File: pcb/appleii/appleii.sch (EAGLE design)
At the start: 21 parts, among them J1 ATX24RH

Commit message: updated IIGS design
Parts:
- added U$14, U$15, U$16, U$17, U$18, U$19, U$20: EDGEPAD, atx4vc:EDGEPAD
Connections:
- net GND: now also U$14.P$1, U$15.P$1, U$16.P$1, U$17.P$1, U$18.P$1, U$19.P$1, U$20.P$1
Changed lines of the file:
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@@
 <part name="U$13" library="atx4vc" deviceset="EDGEPAD" device=""/>
 <part name="GND15" library="supply1" library_urn="urn:adsk.eagle:library:371" deviceset="GND" device=""/>
+<part name="U$14" library="atx4vc" deviceset="EDGEPAD" device=""/>
+<part name="GND16" library="supply1" library_urn="urn:adsk.eagle:library:371" deviceset="GND" device=""/>
+<part name="U$15" library="atx4vc" deviceset="EDGEPAD" device=""/>
+<part name="GND17" library="supply1" library_urn="urn:adsk.eagle:library:371" deviceset="GND" device=""/>
+<part name="U$16" library="atx4vc" deviceset="EDGEPAD" device=""/>
+<part name="GND18" library="supply1" library_urn="urn:adsk.eagle:library:371" deviceset="GND" device=""/>
+<part name="U$17" library="atx4vc" deviceset="EDGEPAD" device=""/>
+<part name="GND19" library="supply1" library_urn="urn:adsk.eagle:library:371" deviceset="GND" device=""/>
+<part name="U$18" library="atx4vc" deviceset="EDGEPAD" device=""/>
+<part name="GND20" library="supply1" library_urn="urn:adsk.eagle:library:371" deviceset="GND" device=""/>
+<part name="U$19" library="atx4vc" deviceset="EDGEPAD" device=""/>
+<part name="GND21" library="supply1" library_urn="urn:adsk.eagle:library:371" deviceset="GND" device=""/>
+<part name="U$20" library="atx4vc" deviceset="EDGEPAD" device=""/>
+<part name="GND22" library="supply1" library_urn="urn:adsk.eagle:library:371" deviceset="GND" device=""/>
 </parts>
 <sheets>
@@
 <instance part="GND15" gate="1" x="73.66" y="25.4" smashed="yes">
 <attribute name="VALUE" x="71.12" y="22.86" size="1.778" layer="96"/>
+</instance>
+<instance part="U$14" gate="G$1" x="175.26" y="53.34" smashed="yes"/>
+<instance part="GND16" gate="1" x="165.1" y="50.8" smashed="yes">
+<attribute name="VALUE" x="162.56" y="48.26" size="1.778" layer="96"/>
+</instance>
+<instance part="U$15" gate="G$1" x="175.26" y="40.64" smashed="yes"/>
+<instance part="GND17" gate="1" x="165.1" y="38.1" smashed="yes">
+<attribute name="VALUE" x="162.56" y="35.56" size="1.778" layer="96"/>
+</instance>
+<instance part="U$16" gate="G$1" x="175.26" y="27.94" smashed="yes"/>
+<instance part="GND18" gate="1" x="165.1" y="25.4" smashed="yes">
+<attribute name="VALUE" x="162.56" y="22.86" size="1.778" layer="96"/>
+</instance>
+<instance part="U$17" gate="G$1" x="175.26" y="15.24" smashed="yes"/>
+<instance part="GND19" gate="1" x="165.1" y="12.7" smashed="yes">
+<attribute name="VALUE" x="162.56" y="10.16" size="1.778" layer="96"/>
+</instance>
+<instance part="U$18" gate="G$1" x="261.62" y="35.56" smashed="yes"/>
+<instance part="GND20" gate="1" x="251.46" y="33.02" smashed="yes">
+<attribute name="VALUE" x="248.92" y="30.48" size="1.778" layer="96"/>
+</instance>
+<instance part="U$19" gate="G$1" x="261.62" y="22.86" smashed="yes"/>
+<instance part="GND21" gate="1" x="251.46" y="20.32" smashed="yes">
+<attribute name="VALUE" x="248.92" y="17.78" size="1.778" layer="96"/>
+</instance>
+<instance part="U$20" gate="G$1" x="261.62" y="10.16" smashed="yes"/>
+<instance part="GND22" gate="1" x="251.46" y="7.62" smashed="yes">
+<attribute name="VALUE" x="248.92" y="5.08" size="1.778" layer="96"/>
 </instance>
 </instances>
@@
 <wire x1="73.66" y1="27.94" x2="78.74" y2="27.94" width="0.1524" layer="91"/>
 </segment>
+<segment>
+<pinref part="GND16" gate="1" pin="GND"/>
+<pinref part="U$14" gate="G$1" pin="P$1"/>
+<wire x1="165.1" y1="53.34" x2="170.18" y2="53.34" width="0.1524" layer="91"/>
+</segment>
+<segment>
+<pinref part="GND17" gate="1" pin="GND"/>
+<pinref part="U$15" gate="G$1" pin="P$1"/>
+<wire x1="165.1" y1="40.64" x2="170.18" y2="40.64" width="0.1524" layer="91"/>
+</segment>
+<segment>
+<pinref part="GND18" gate="1" pin="GND"/>
+<pinref part="U$16" gate="G$1" pin="P$1"/>
+<wire x1="165.1" y1="27.94" x2="170.18" y2="27.94" width="0.1524" layer="91"/>
+</segment>
+<segment>
+<pinref part="GND19" gate="1" pin="GND"/>
+<pinref part="U$17" gate="G$1" pin="P$1"/>
+<wire x1="165.1" y1="15.24" x2="170.18" y2="15.24" width="0.1524" layer="91"/>
+</segment>
+<segment>
+<pinref part="GND20" gate="1" pin="GND"/>
+<pinref part="U$18" gate="G$1" pin="P$1"/>
+<wire x1="251.46" y1="35.56" x2="256.54" y2="35.56" width="0.1524" layer="91"/>
+</segment>
+<segment>
+<pinref part="GND21" gate="1" pin="GND"/>
+<pinref part="U$19" gate="G$1" pin="P$1"/>
+<wire x1="251.46" y1="22.86" x2="256.54" y2="22.86" width="0.1524" layer="91"/>
+</segment>
+<segment>
+<pinref part="GND22" gate="1" pin="GND"/>
+<pinref part="U$20" gate="G$1" pin="P$1"/>
+<wire x1="251.46" y1="10.16" x2="256.54" y2="10.16" width="0.1524" layer="91"/>
+</segment>
 </net>

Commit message: added more caps
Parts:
- removed C1: (no value), capacitor-wima:C5/2.5
- removed JP1: (no value), pinhead:PINHD-1X2
- added C5, C7, C8, C9: (no value), capacitor-wima:C5/2.5
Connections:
- net +12V: now also C9.1
- net +5V: now also C7.1, C8.1
- net GND: now also C5.2, C7.2, C8.2, C9.2; no longer C1.2, JP1.2
- net N$5: no longer JP1.1
- net N$6: no longer C1.1
- net N$8: now also C5.1
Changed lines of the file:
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@@
 <?xml version="1.0" encoding="utf-8"?>
 <!DOCTYPE eagle SYSTEM "eagle.dtd">
-<eagle version="9.6.1">
+<eagle version="9.6.2">
 <drawing>
 <settings>
@@
 <part name="U$1" library="atx_power_control" deviceset="CAR_FUSE_HOLDER" device="3IN1"/>
 <part name="U$2" library="atx_power_control" deviceset="CAR_FUSE_HOLDER" device="3IN1"/>
-<part name="JP1" library="pinhead" library_urn="urn:adsk.eagle:library:325" deviceset="PINHD-1X2" device="" package3d_urn="urn:adsk.eagle:package:22435/2"/>
 <part name="P+3" library="supply1" library_urn="urn:adsk.eagle:library:371" deviceset="+5V" device=""/>
 <part name="GND3" library="supply1" library_urn="urn:adsk.eagle:library:371" deviceset="GND" device=""/>
@@
 <part name="P-5" library="supply1" library_urn="urn:adsk.eagle:library:371" deviceset="-5V" device=""/>
 <part name="C2" library="capacitor-wima" library_urn="urn:adsk.eagle:library:116" deviceset="C" device="5/2.5" package3d_urn="urn:adsk.eagle:package:5426/1"/>
-<part name="C1" library="capacitor-wima" library_urn="urn:adsk.eagle:library:116" deviceset="C" device="5/2.5" package3d_urn="urn:adsk.eagle:package:5426/1"/>
-<part name="GND9" library="supply1" library_urn="urn:adsk.eagle:library:371" deviceset="GND" device=""/>
 <part name="GND10" library="supply1" library_urn="urn:adsk.eagle:library:371" deviceset="GND" device=""/>
 <part name="C3" library="capacitor-wima" library_urn="urn:adsk.eagle:library:116" deviceset="C" device="5/2.5" package3d_urn="urn:adsk.eagle:package:5426/1"/>
@@
 <part name="U$20" library="atx4vc" deviceset="EDGEPAD" device=""/>
 <part name="GND22" library="supply1" library_urn="urn:adsk.eagle:library:371" deviceset="GND" device=""/>
+<part name="C5" library="capacitor-wima" library_urn="urn:adsk.eagle:library:116" deviceset="C" device="5/2.5" package3d_urn="urn:adsk.eagle:package:5426/1"/>
+<part name="GND23" library="supply1" library_urn="urn:adsk.eagle:library:371" deviceset="GND" device=""/>
+<part name="C7" library="capacitor-wima" library_urn="urn:adsk.eagle:library:116" deviceset="C" device="5/2.5" package3d_urn="urn:adsk.eagle:package:5426/1"/>
+<part name="C8" library="capacitor-wima" library_urn="urn:adsk.eagle:library:116" deviceset="C" device="5/2.5" package3d_urn="urn:adsk.eagle:package:5426/1"/>
+<part name="GND24" library="supply1" library_urn="urn:adsk.eagle:library:371" deviceset="GND" device=""/>
+<part name="C9" library="capacitor-wima" library_urn="urn:adsk.eagle:library:116" deviceset="C" device="5/2.5" package3d_urn="urn:adsk.eagle:package:5426/1"/>
+<part name="GND25" library="supply1" library_urn="urn:adsk.eagle:library:371" deviceset="GND" device=""/>
 </parts>
 <sheets>
@@
 <instance part="U$1" gate="G$1" x="38.1" y="187.96" smashed="yes"/>
 <instance part="U$2" gate="G$1" x="154.94" y="175.26" smashed="yes"/>
-<instance part="JP1" gate="G$1" x="180.34" y="160.02" smashed="yes">
-<attribute name="NAME" x="173.99" y="165.735" size="1.778" layer="95"/>
-<attribute name="VALUE" x="173.99" y="154.94" size="1.778" layer="96"/>
-</instance>
 <instance part="P+3" gate="1" x="12.7" y="193.04" smashed="yes">
 <attribute name="VALUE" x="10.16" y="187.96" size="1.778" layer="96" rot="R90"/>
@@
 <attribute name="VALUE" x="133.604" y="168.021" size="1.778" layer="96"/>
 </instance>
-<instance part="C1" gate="G$1" x="58.42" y="185.42" smashed="yes">
-<attribute name="NAME" x="59.944" y="185.801" size="1.778" layer="95"/>
-<attribute name="VALUE" x="59.944" y="180.721" size="1.778" layer="96"/>
-</instance>
-<instance part="GND9" gate="1" x="58.42" y="177.8" smashed="yes">
-<attribute name="VALUE" x="55.88" y="175.26" size="1.778" layer="96"/>
-</instance>
 <instance part="GND10" gate="1" x="132.08" y="165.1" smashed="yes">
 <attribute name="VALUE" x="129.54" y="162.56" size="1.778" layer="96"/>
@@
 <instance part="GND22" gate="1" x="251.46" y="7.62" smashed="yes">
 <attribute name="VALUE" x="248.92" y="5.08" size="1.778" layer="96"/>
+</instance>
+<instance part="C5" gate="G$1" x="127" y="172.72" smashed="yes">
+<attribute name="NAME" x="128.524" y="173.101" size="1.778" layer="95"/>
+<attribute name="VALUE" x="128.524" y="168.021" size="1.778" layer="96"/>
+</instance>
+<instance part="GND23" gate="1" x="127" y="165.1" smashed="yes">
+<attribute name="VALUE" x="124.46" y="162.56" size="1.778" layer="96"/>
+</instance>
+<instance part="C7" gate="G$1" x="20.32" y="177.8" smashed="yes">
+<attribute name="NAME" x="21.844" y="178.181" size="1.778" layer="95"/>
+<attribute name="VALUE" x="21.844" y="173.101" size="1.778" layer="96"/>
+</instance>
+<instance part="C8" gate="G$1" x="12.7" y="177.8" smashed="yes">
+<attribute name="NAME" x="14.224" y="178.181" size="1.778" layer="95"/>
+<attribute name="VALUE" x="14.224" y="173.101" size="1.778" layer="96"/>
+</instance>
+<instance part="GND24" gate="1" x="12.7" y="167.64" smashed="yes">
+<attribute name="VALUE" x="10.16" y="165.1" size="1.778" layer="96"/>
+</instance>
+<instance part="C9" gate="G$1" x="193.04" y="172.72" smashed="yes">
+<attribute name="NAME" x="194.564" y="173.101" size="1.778" layer="95"/>
+<attribute name="VALUE" x="194.564" y="168.021" size="1.778" layer="96"/>
+</instance>
+<instance part="GND25" gate="1" x="193.04" y="165.1" smashed="yes">
+<attribute name="VALUE" x="190.5" y="162.56" size="1.778" layer="96"/>
 </instance>
 </instances>
@@
 <segment>
 <pinref part="GND3" gate="1" pin="GND"/>
-<pinref part="JP1" gate="G$1" pin="2"/>
-<wire x1="149.86" y1="160.02" x2="177.8" y2="160.02" width="0.1524" layer="91"/>
-<wire x1="177.8" y1="160.02" x2="215.9" y2="160.02" width="0.1524" layer="91"/>
+<wire x1="149.86" y1="160.02" x2="215.9" y2="160.02" width="0.1524" layer="91"/>
 <wire x1="215.9" y1="160.02" x2="215.9" y2="149.86" width="0.1524" layer="91"/>
-<junction x="177.8" y="160.02"/>
 <pinref part="U$3" gate="G$1" pin="P$3"/>
 <pinref part="U$3" gate="G$1" pin="P$1"/>
@@
 </segment>
 <segment>
-<pinref part="C1" gate="G$1" pin="2"/>
-<pinref part="GND9" gate="1" pin="GND"/>
-</segment>
-<segment>
 <pinref part="C2" gate="G$1" pin="2"/>
 <pinref part="GND10" gate="1" pin="GND"/>
@@
 <pinref part="U$20" gate="G$1" pin="P$1"/>
 <wire x1="251.46" y1="10.16" x2="256.54" y2="10.16" width="0.1524" layer="91"/>
+</segment>
+<segment>
+<pinref part="C5" gate="G$1" pin="2"/>
+<pinref part="GND23" gate="1" pin="GND"/>
+</segment>
+<segment>
+<pinref part="C8" gate="G$1" pin="2"/>
+<pinref part="GND24" gate="1" pin="GND"/>
+<wire x1="12.7" y1="172.72" x2="12.7" y2="170.18" width="0.1524" layer="91"/>
+<pinref part="C7" gate="G$1" pin="2"/>
+<wire x1="12.7" y1="172.72" x2="20.32" y2="172.72" width="0.1524" layer="91"/>
+<junction x="12.7" y="172.72"/>
+</segment>
+<segment>
+<pinref part="C9" gate="G$1" pin="2"/>
+<pinref part="GND25" gate="1" pin="GND"/>
 </segment>
 </net>
@@
 <pinref part="J1" gate="G$1" pin="5V@3"/>
 <pinref part="J1" gate="G$1" pin="5V@4"/>
-<pinref part="C1" gate="G$1" pin="1"/>
-<wire x1="53.594" y1="189.23" x2="58.42" y2="189.23" width="0.1524" layer="91"/>
-<wire x1="58.42" y1="189.23" x2="58.42" y2="187.96" width="0.1524" layer="91"/>
 </segment>
 </net>
@@
 <wire x1="12.7" y1="189.23" x2="12.7" y2="190.5" width="0.1524" layer="91"/>
 <junction x="23.114" y="189.23"/>
+<pinref part="C8" gate="G$1" pin="1"/>
+<wire x1="12.7" y1="180.34" x2="12.7" y2="190.5" width="0.1524" layer="91"/>
+<junction x="12.7" y="190.5"/>
+<pinref part="C7" gate="G$1" pin="1"/>
+<wire x1="20.32" y1="180.34" x2="12.7" y2="180.34" width="0.1524" layer="91"/>
+<junction x="12.7" y="180.34"/>
 </segment>
 <segment>
@@
 <pinref part="J1" gate="G$1" pin="12V@1"/>
 <pinref part="C2" gate="G$1" pin="1"/>
-<wire x1="121.92" y1="175.26" x2="132.08" y2="175.26" width="0.1524" layer="91"/>
+<wire x1="121.92" y1="175.26" x2="127" y2="175.26" width="0.1524" layer="91"/>
+<pinref part="C5" gate="G$1" pin="1"/>
+<wire x1="127" y1="175.26" x2="132.08" y2="175.26" width="0.1524" layer="91"/>
+<junction x="127" y="175.26"/>
 </segment>
 </net>
@@
 <wire x1="170.434" y1="173.99" x2="170.434" y2="176.53" width="0.1524" layer="91"/>
 <junction x="170.434" y="176.53"/>
+<pinref part="C9" gate="G$1" pin="1"/>
+<wire x1="193.04" y1="175.26" x2="193.04" y2="177.8" width="0.1524" layer="91"/>
+<wire x1="193.04" y1="177.8" x2="180.34" y2="177.8" width="0.1524" layer="91"/>
+<junction x="180.34" y="177.8"/>
 </segment>
 <segment>
@@
 <net name="N$5" class="0">
 <segment>
-<wire x1="109.22" y1="162.56" x2="177.8" y2="162.56" width="0.1524" layer="91"/>
-<pinref part="JP1" gate="G$1" pin="1"/>
+<wire x1="109.22" y1="162.56" x2="215.9" y2="162.56" width="0.1524" layer="91"/>
 <pinref part="J1" gate="G$1" pin="PS_ON"/>
-<wire x1="177.8" y1="162.56" x2="215.9" y2="162.56" width="0.1524" layer="91"/>
 <wire x1="215.9" y1="162.56" x2="215.9" y2="172.72" width="0.1524" layer="91"/>
-<junction x="177.8" y="162.56"/>
 <pinref part="U$3" gate="G$1" pin="P$2"/>
 <pinref part="U$3" gate="G$1" pin="P$4"/>

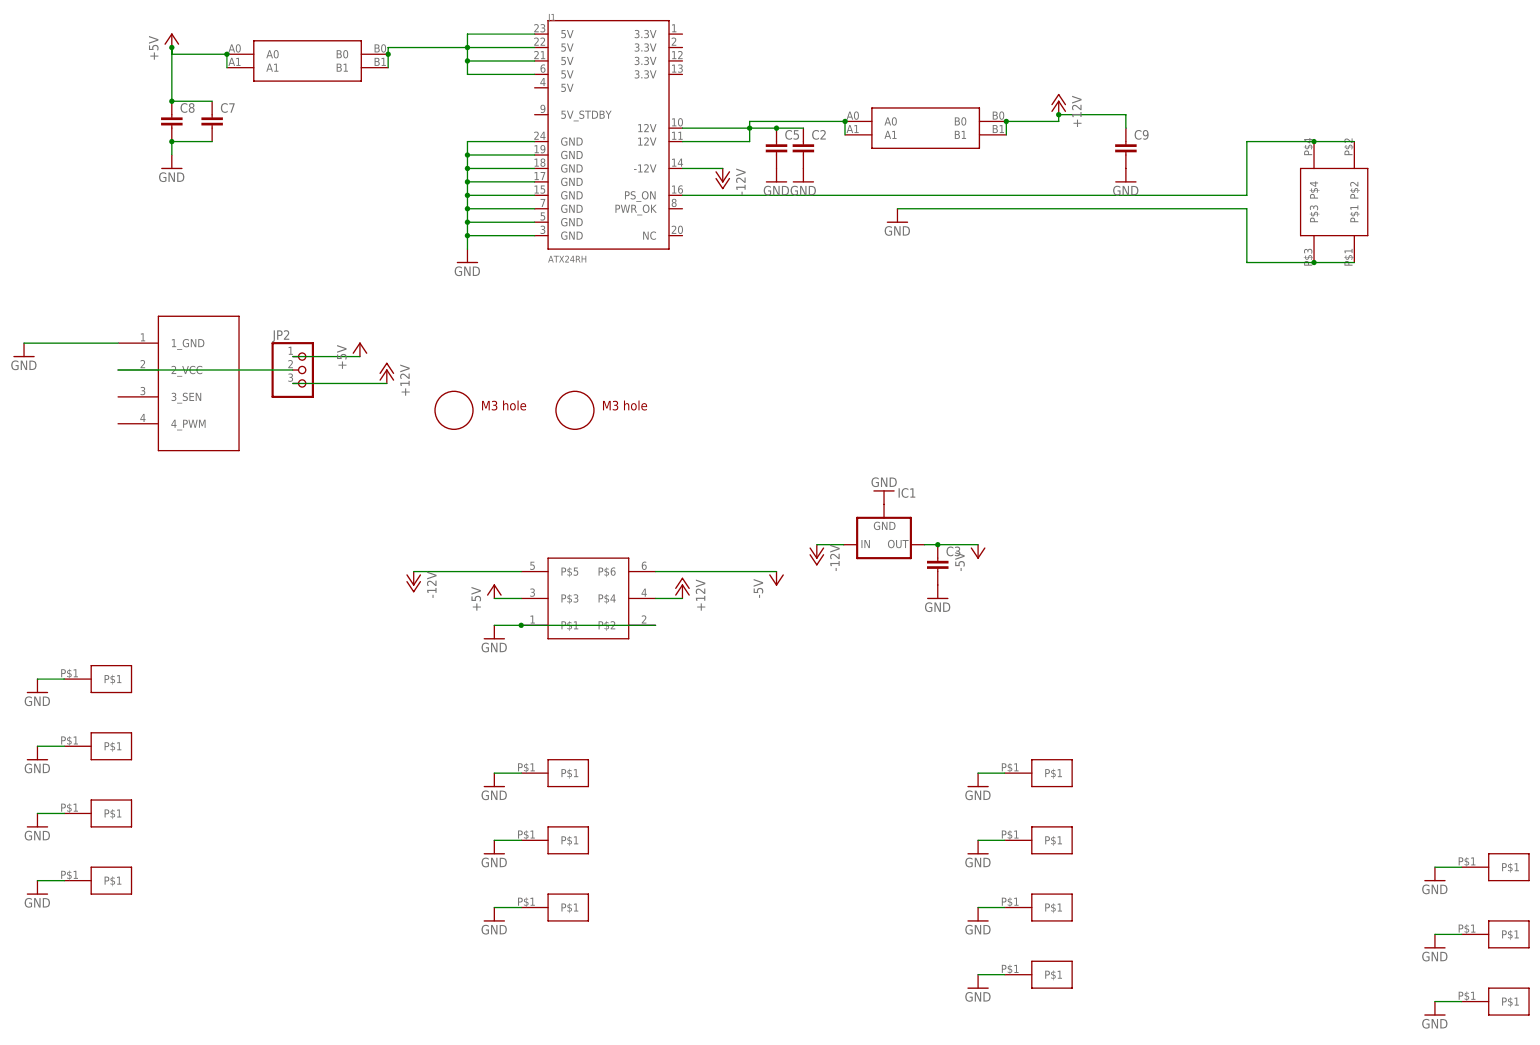
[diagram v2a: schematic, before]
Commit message: changed to 70L05
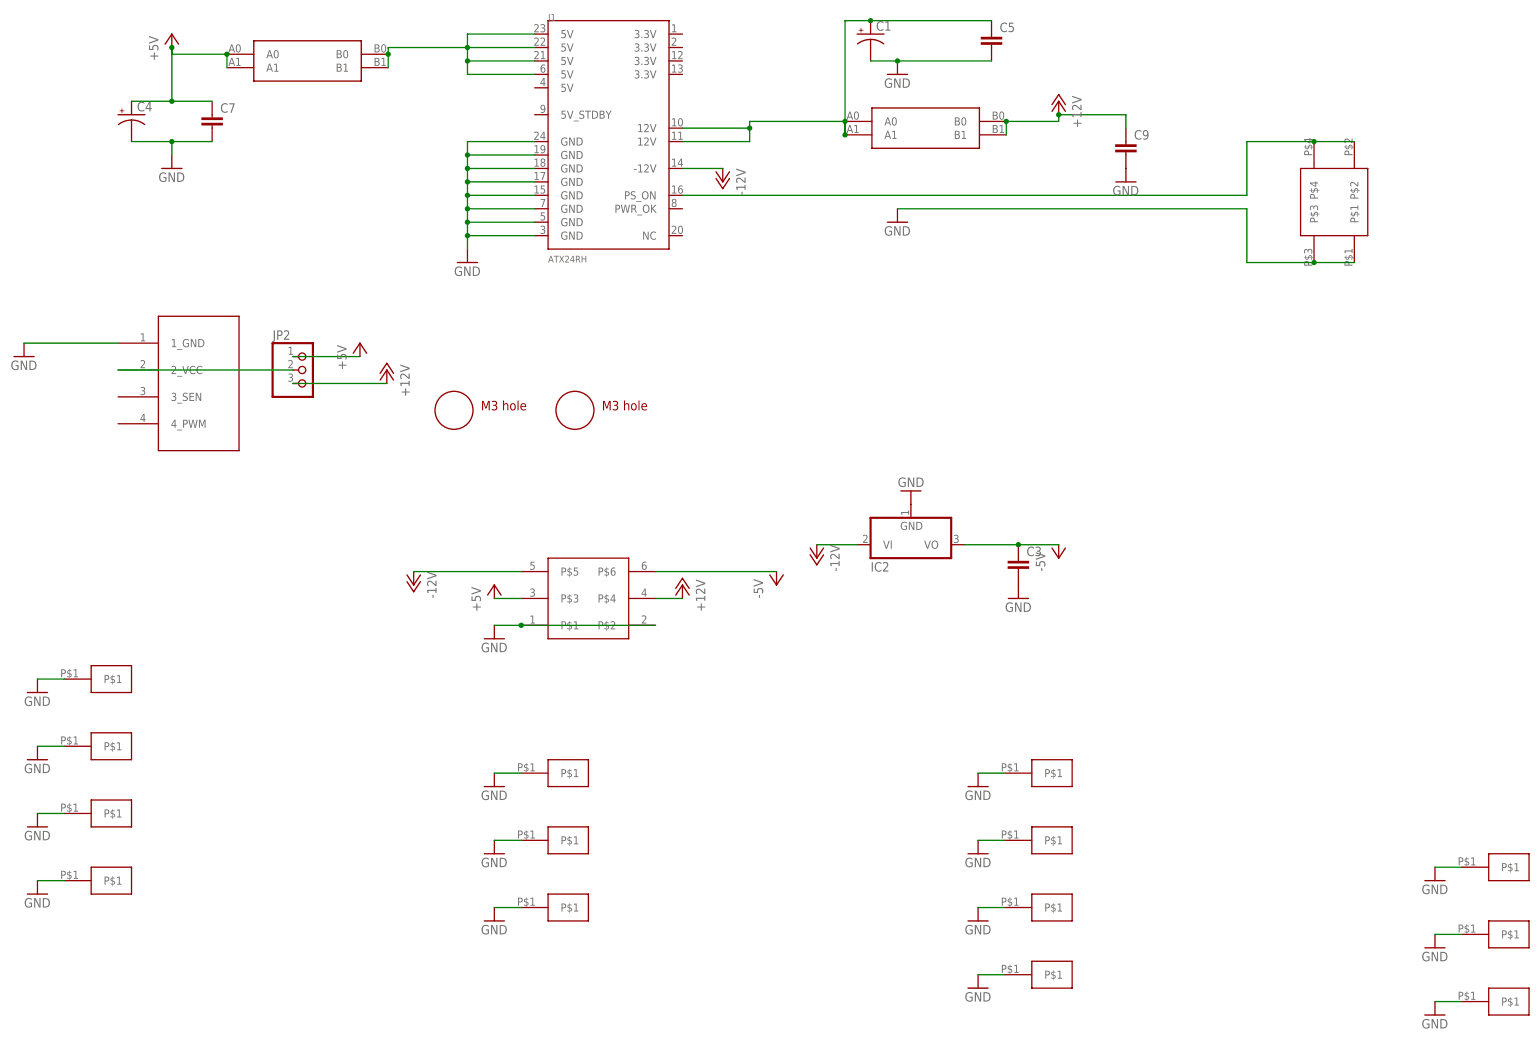
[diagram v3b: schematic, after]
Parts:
- removed C2, C8: (no value), capacitor-wima:C5/2.5
- removed IC1: (no value), v-reg:79XXS
- added C1, C4: (no value), adafruit:CPOL-USE5-10.5
- added IC2: (no value), linear:7905L
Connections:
- net +5V: now also C4.+; no longer C8.1
- net -12V: now also IC2.VI; no longer IC1.IN
- net -5V: now also IC2.VO; no longer IC1.OUT
- net GND: now also C1.-, C4.-, IC2.GND; no longer C2.2, C8.2, IC1.GND
- net N$8: now also C1.+; no longer C2.1
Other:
- moved on the sheet: C3, C5
